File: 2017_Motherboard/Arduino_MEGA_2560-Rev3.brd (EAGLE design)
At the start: 100 x 78 mm, 100 parts, among them IC1 NCP1117ST50T3G, IC2 FT232RL, IC3 ATMEGA2560-16AU, IC4 MAX4312ESE, IC5 MAX3468CPA, IC6 MAX4312ESE, IC7 LMV358IDGKR, X1 POWERSUPPLY_DC21MMX, Y1 CSTCE16M0V53-R0 16MHZ

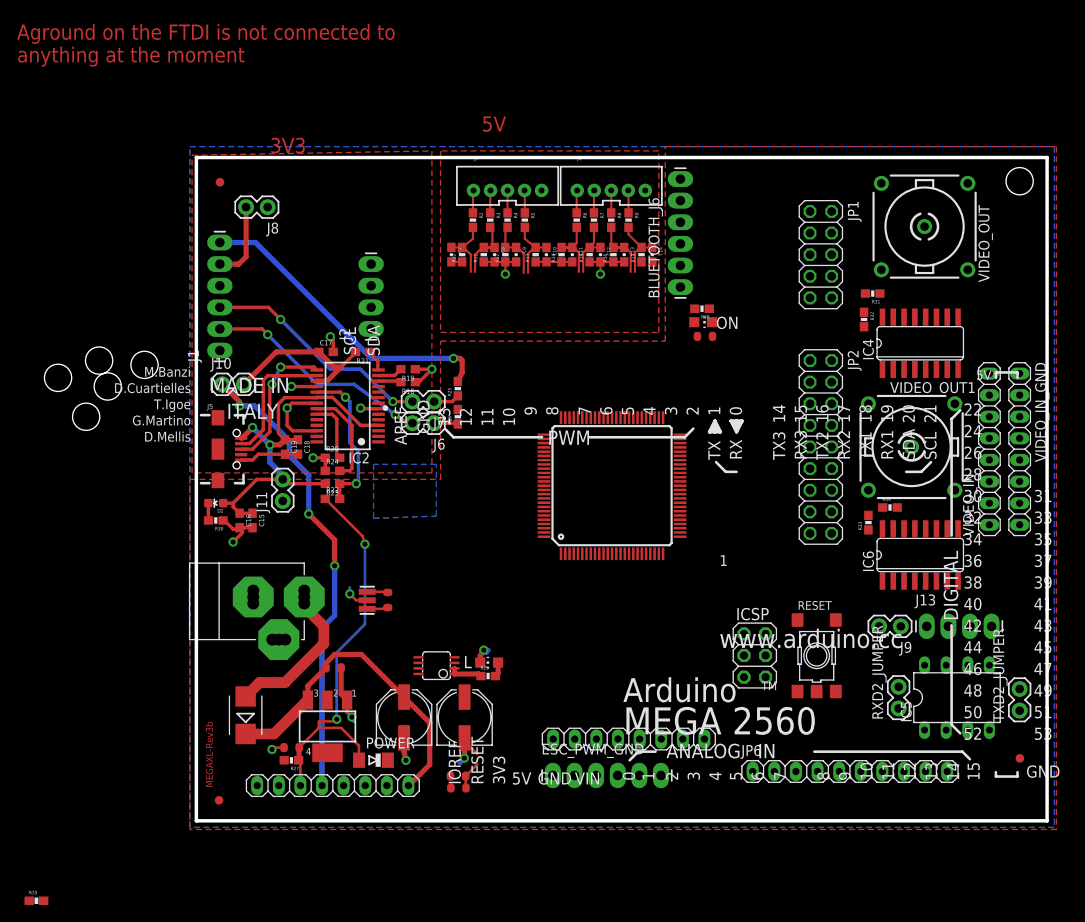
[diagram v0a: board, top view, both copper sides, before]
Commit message: Half of routing done
fixed errors in ERC, removed op amp on pin 13, disconnected AREF and
changed to AGND. AGND separated from GND by 1M resistor. Video routing
TBD. AGND plane TBD?
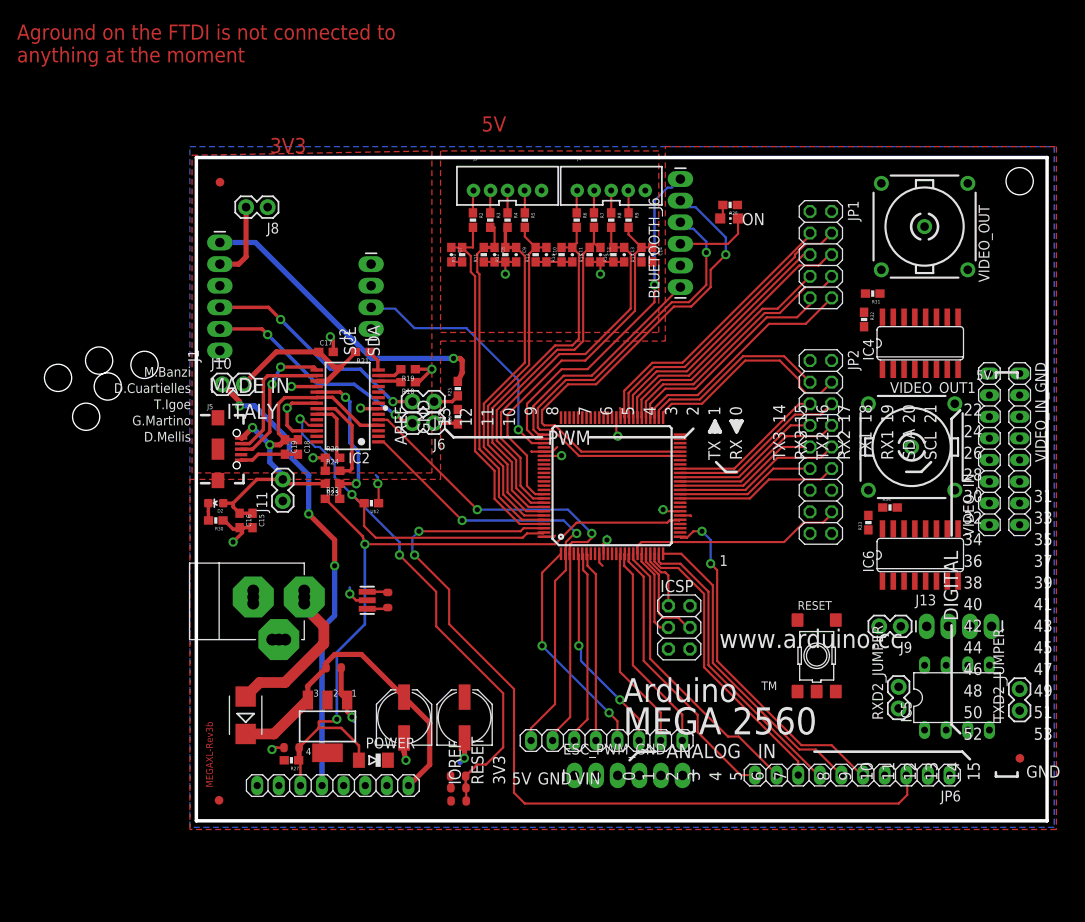
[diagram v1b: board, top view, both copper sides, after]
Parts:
- removed IC7: LMV358IDGKR, linear:MSOP08
- removed L: YELLOW, led:CHIP-LED0805
- removed R29: 1K, SparkFun-Resistors:0603-RES
- removed R35: (no value), SparkFun-Passives:0603-RES
- added U$2: 1M, SparkFun-Resistors:0603-RES
- moved C5 61.8 mm to (30.8, 2.33)
- moved R28 12.6 mm to (62.7, 72.4)
- moved ON 12.6 mm to (62.6, 70.8)
- moved ICSP 9.48 mm to (56.8, 22.7)
- moved PWML 2.61 mm to (48.2, 9.44), turned to 0 degrees
- moved ESC_PWM_GND 2.54 mm to (44.5, 5.33)
- moved JP6 0.50 mm to (77.1, 5.38), turned to 180 degrees
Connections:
- removed net FB: IC4.15, IC6.15
- removed net L13: IC7.1, IC7.2, R29.1
- removed net N$16: JP6.2
- removed net N$2: L.A, R29.2
- removed net V+: IC7.8
- removed net V-: IC7.4
- new net AGND: C4.2, C5.2, C6.2, IC2.25, IC3.99, U$2.2
- net AREF: no longer IC2.25, R35.2
- net GND: now also U$2.1; no longer C4.2, C5.2, C6.2, IC3.99, L.C, R35.1
- net N$17: now also IC4.15
- net N$18: now also IC6.15
- net PB7: no longer IC7.3
- net SDA: now also JP6.2
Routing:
- net AREF: track 0.00 -> 100.4 mm, vias 0 -> 2
- net AGND: track 0.00 -> 86.4 mm, vias 0 -> 3
- net TXD1: track 0.00 -> 58.6 mm, vias 0 -> 1
- net PE1: track 0.00 -> 58.0 mm, vias 0 -> 2
- net RXD1: track 0.00 -> 55.3 mm, vias 0 -> 1
- net PE0: track 0.00 -> 54.5 mm, vias 0 -> 2
- net PB7: track 0.00 -> 41.6 mm, vias 0 -> 2
- net PA1: track 0.00 -> 41.5 mm, vias 0 -> 1
- net RESET: track 47.4 -> 85.6 mm
- net PB6: track 0.00 -> 37.1 mm
- net ADC7: track 7.56 -> 44.2 mm
- net ADC6: track 8.30 -> 44.5 mm
- net ADC0: track 7.62 -> 43.1 mm
- net ADC5: track 7.14 -> 42.5 mm
- net PB5: track 0.00 -> 35.3 mm
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- removed copper zone on layer 16, net AREF

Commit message: slight routing additions
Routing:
- net PB0: track 25.6 -> 27.4 mm
